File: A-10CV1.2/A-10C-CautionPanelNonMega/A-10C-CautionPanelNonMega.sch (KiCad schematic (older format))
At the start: 31 parts, among them J1 Barrel_Jack, J10 Conn_01x24, J11 Conn_01x24, J13 Conn_01x03, J2 Nano Pins 1-15, J3 Nano Pins 16-30 (reversed), J4 Serial Tx/Rx, J8 Conn_01x24, J9 Conn_01x24, Q1 BC338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

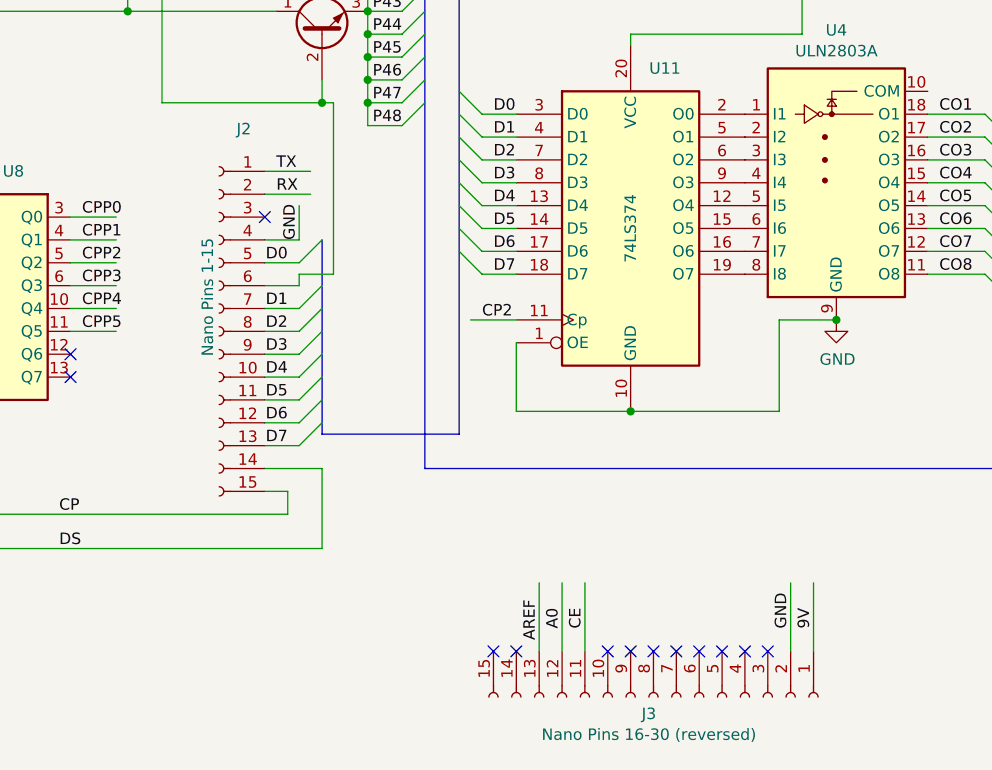
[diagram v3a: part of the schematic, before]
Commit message: Updated Anano Pin Labels
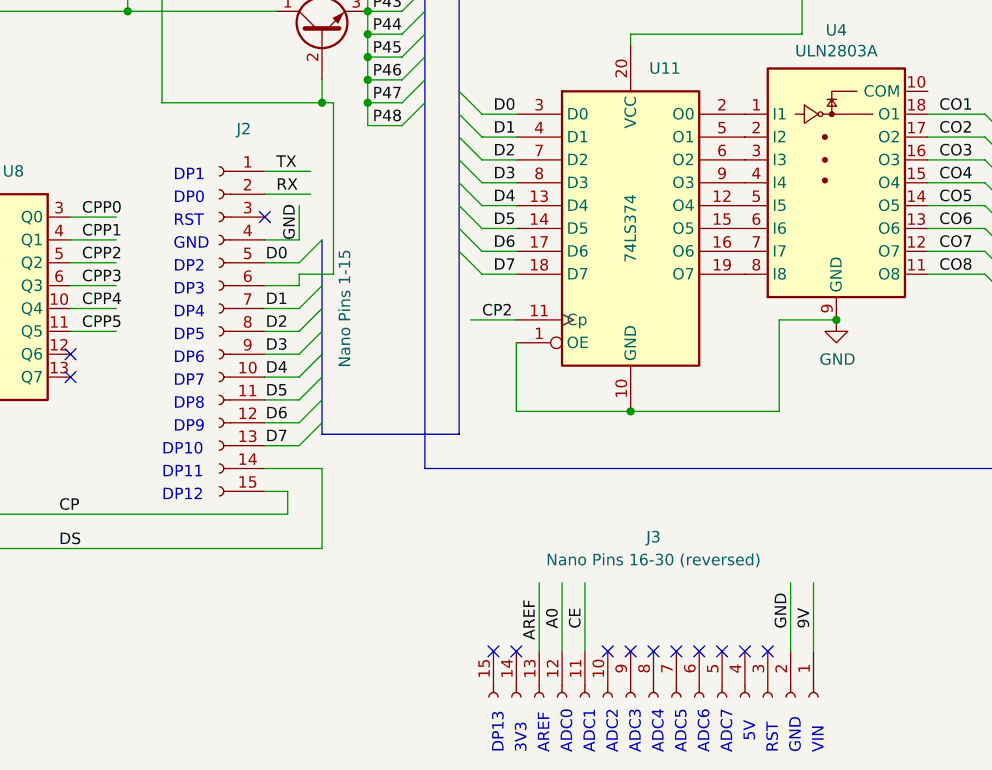
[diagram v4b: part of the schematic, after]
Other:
- note added: "3V3"
- note added: "5V"
- note added: "ADC0"
- note added: "ADC1"
- note added: "ADC2"
- note added: "ADC3"
- note added: "ADC4"
- note added: "ADC5"
- note added: "ADC6"
- note added: "ADC7"
- note added: "AREF"
- note added: "DP0"
- note added: "DP1"
- note added: "DP10"
- note added: "DP11"
- note added: "DP12"
- note added: "DP13"
- note added: "DP2"
- note added: "DP3"
- note added: "DP4"
- note added: "DP5"
- note added: "DP6"
- note added: "DP7"
- note added: "DP8"
- note added: "DP9"
- note added: "GND"
- note added: "RST"
- note added: "VIN"
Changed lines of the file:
@@
 Sheet 1 1
 Title "A-10C-Caution Panel Driver/Interface Board"
-Date "2019-10-26"
+Date "2019-11-06"
 Rev "1.0"
 Comp "IzeHouze"
@@
 P 2350 5950
 F 0 "J2" H 2242 6835 50  0000 C CNN
-F 1 "Nano Pins 1-15" V 2400 6100 50  0000 C CNN
+F 1 "Nano Pins 1-15" V 1800 6050 50  0000 C CNN
 F 2 "Connector_PinSocket_2.54mm:PinSocket_1x15_P2.54mm_Vertical" H 2350 5950 50  0001 C CNN
 F 3 "~" H 2350 5950 50  0001 C CNN
@@
 U 1 1 6133F9F4
 P 4250 7550
-F 0 "J3" V 4323 7530 50  0000 C CNN
-F 1 "Nano Pins 16-30 (reversed)" V 4414 7530 50  0000 C CNN
+F 0 "J3" V 3550 7550 50  0000 C CNN
+F 1 "Nano Pins 16-30 (reversed)" V 3650 7550 50  0000 C CNN
 F 2 "Connector_PinSocket_2.54mm:PinSocket_1x15_P2.54mm_Vertical" H 4250 7550 50  0001 C CNN
 F 3 "~" H 4250 7550 50  0001 C CNN
@@
 Wire Wire Line
 	2800 2600 3000 2600
+Text Label 1650 6750 0    50   ~ 0
+CP
+Text Label 1650 6900 0    50   ~ 0
+DS
+Text Notes 2150 5800 0    50   ~ 0
+DP3
+Text Notes 2150 5900 0    50   ~ 0
+DP4
+Text Notes 2150 6000 0    50   ~ 0
+DP5
+Text Notes 2150 6100 0    50   ~ 0
+DP6
+Text Notes 2150 6200 0    50   ~ 0
+DP7
+Text Notes 2150 6300 0    50   ~ 0
+DP8
+Text Notes 2150 6400 0    50   ~ 0
+DP9
+Text Notes 2100 6500 0    50   ~ 0
+DP10
+Text Notes 2150 5600 0    50   ~ 0
+GND
+Text Notes 2150 5700 0    50   ~ 0
+DP2
+Text Notes 2150 5500 0    50   ~ 0
+RST
+Text Notes 2150 5400 0    50   ~ 0
+DP0
+Text Notes 2150 5300 0    50   ~ 0
+DP1
+Text Notes 2100 6600 0    50   ~ 0
+DP11
+Text Notes 2100 6700 0    50   ~ 0
+DP12
+Text Notes 3600 7800 1    50   ~ 0
+DP13
+Text Notes 3700 7800 1    50   ~ 0
+3V3
+Text Notes 3800 7800 1    50   ~ 0
+AREF
+Text Notes 3900 7800 1    50   ~ 0
+ADC0
+Text Notes 4000 7800 1    50   ~ 0
+ADC1
+Text Notes 4100 7800 1    50   ~ 0
+ADC2
+Text Notes 4200 7800 1    50   ~ 0
+ADC3
+Text Notes 4300 7800 1    50   ~ 0
+ADC4
+Text Notes 4400 7800 1    50   ~ 0
+ADC5
+Text Notes 4500 7800 1    50   ~ 0
+ADC6
+Text Notes 4600 7800 1    50   ~ 0
+ADC7
 Wire Bus Line
 	2800 5550 2800 6400
@@
 Wire Bus Line
 	9550 750  9550 6550
-Text Label 1650 6750 0    50   ~ 0
-CP
-Text Label 1650 6900 0    50   ~ 0
-DS
+Text Notes 4700 7750 1    50   ~ 0
+5V
+Text Notes 4800 7800 1    50   ~ 0
+RST
+Text Notes 4900 7800 1    50   ~ 0
+GND
+Text Notes 5000 7800 1    50   ~ 0
+VIN
 $EndSCHEMATC

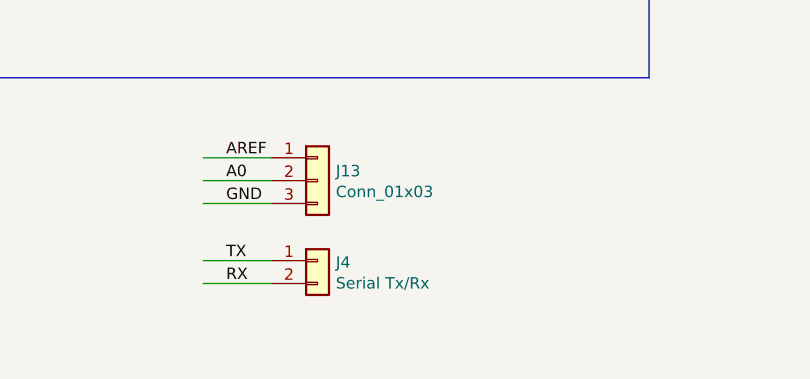
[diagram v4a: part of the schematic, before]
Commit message: Updating RS port to three pin
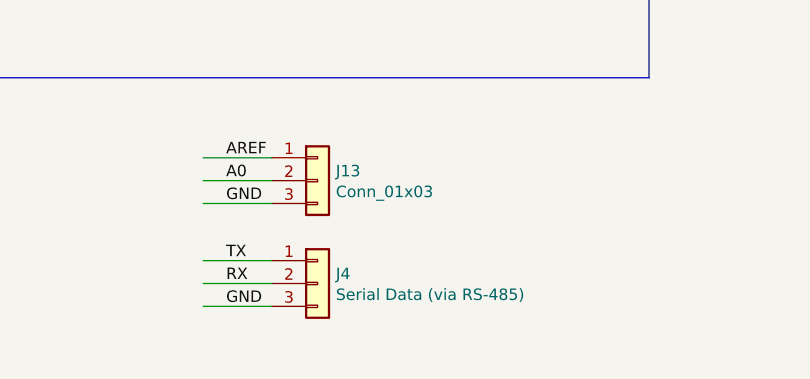
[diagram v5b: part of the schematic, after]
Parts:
- removed J4: Serial Tx/Rx, Connector_PinHeader_2.54mm:PinHeader_1x02_P2.54mm_Vertical, symbol Connector_Generic:Conn_01x02
- added J4: Serial Data (via RS-485), Connector_PinHeader_2.54mm:PinHeader_1x03_P2.54mm_Vertical, symbol Connector_Generic:Conn_01x03
- U15, U16: footprint (none) -> Package_DIP:DIP-14_W7.62mm
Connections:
- wire segments 434 -> 435
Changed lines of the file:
@@
 Text Label 2600 5350 0    50   ~ 0
 RX
-$Comp
-L Connector_Generic:Conn_01x02 J4
-U 1 1 5DFBAF06
-P 8100 7350
-F 0 "J4" H 8180 7342 50  0000 L CNN
-F 1 "Serial Tx/Rx" H 8180 7251 50  0000 L CNN
-F 2 "Connector_PinHeader_2.54mm:PinHeader_1x02_P2.54mm_Vertical" H 8100 7350 50  0001 C CNN
-F 3 "~" H 8100 7350 50  0001 C CNN
-	1    8100 7350
-	1    0    0    -1
-$EndComp
 Wire Wire Line
 	7900 7350 7600 7350
@@
 F 0 "U15" V 11333 5750 50  0000 C CNN
 F 1 "74LS08" V 11424 5750 50  0000 C CNN
-F 2 "" H 11700 5750 50  0001 C CNN
+F 2 "Package_DIP:DIP-14_W7.62mm" H 11700 5750 50  0001 C CNN
 F 3 "http://www.ti.com/lit/gpn/sn74LS08" H 11700 5750 50  0001 C CNN
 	5    11700 5750
@@
 F 0 "U16" V 11333 6400 50  0000 C CNN
 F 1 "74LS08" V 11424 6400 50  0000 C CNN
-F 2 "" H 11700 6400 50  0001 C CNN
+F 2 "Package_DIP:DIP-14_W7.62mm" H 11700 6400 50  0001 C CNN
 F 3 "http://www.ti.com/lit/gpn/sn74LS08" H 11700 6400 50  0001 C CNN
 	5    11700 6400
@@
 Text Notes 4600 7800 1    50   ~ 0
 ADC7
-Wire Bus Line
-	2800 5550 2800 6400
-Wire Bus Line
-	5800 1450 5800 5850
-Wire Bus Line
-	2900 600  2900 4050
-Wire Bus Line
-	3250 600  3250 6550
-Wire Bus Line
-	3400 850  3400 6400
-Wire Bus Line
-	6150 850  6150 5250
-Wire Bus Line
-	8500 750  8500 5850
-Wire Bus Line
-	9550 750  9550 6550
 Text Notes 4700 7750 1    50   ~ 0
 5V
@@
 Text Notes 5000 7800 1    50   ~ 0
 VIN
+$Comp
+L Connector_Generic:Conn_01x03 J4
+U 1 1 5DE08373
+P 8100 7450
+F 0 "J4" H 8180 7492 50  0000 L CNN
+F 1 "Serial Data (via RS-485)" H 8180 7401 50  0000 L CNN
+F 2 "Connector_PinHeader_2.54mm:PinHeader_1x03_P2.54mm_Vertical" H 8100 7450 50  0001 C CNN
+F 3 "~" H 8100 7450 50  0001 C CNN
+	1    8100 7450
+	1    0    0    -1
+$EndComp
+Wire Wire Line
+	7900 7550 7600 7550
+Wire Bus Line
+	2800 5550 2800 6400
+Wire Bus Line
+	5800 1450 5800 5850
+Wire Bus Line
+	2900 600  2900 4050
+Wire Bus Line
+	3250 600  3250 6550
+Wire Bus Line
+	3400 850  3400 6400
+Wire Bus Line
+	6150 850  6150 5250
+Wire Bus Line
+	8500 750  8500 5850
+Wire Bus Line
+	9550 750  9550 6550
+Text Label 7700 7550 0    50   ~ 0
+GND
 $EndSCHEMATC
